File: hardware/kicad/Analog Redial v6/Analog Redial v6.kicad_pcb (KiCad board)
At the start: 2 copper layers, 115 x 52 mm, 76 parts, among them J1 Barrel_Jack_PTH_Slot, J2 PINHD_1x8_Male, J3 PINHD_1x2_Male, J4 PINHD_1x2_Male, J5 PINHD_2x4_Male, J7 PINHD_1x3_Male, J8 RJ12, J9 RJ12, U1 ESP32-C6-DevKitC-1, U2 ES8388, U3 AG1171, U4 AG1171, U5 XC6206PxxxMR

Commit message: v6 board: layout and schematic updates, PCBWay production files (Oct 5)
Co-Authored-By: Claude Sonnet 5.5 <noreply@anthropic.com>
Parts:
- removed REF**: OSHW-Logo2_14.6x12mm_SilkScreen, Symbol:OSHW-Logo2_14.6x12mm_SilkScreen
- Card1: value TF-01A -> TF-SMD_TF-01A; footprint JLCImport:TF-01A -> EasyEDA2Kicad:TF-SMD_TF-01A
- U5: value XC6206PxxxMR -> XC6206P362MR
- moved C19 9.90 mm to (108.6, 63.9)
- moved C24 4.83 mm to (71.0, 78.8)
- moved C22 4.75 mm to (73.6, 78.8)
- moved D2 2.50 mm to (89.0, 52.0)
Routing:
- net +5V: track 147.9 -> 150.7 mm, vias 8 -> 7
- net Net-(D2-A): track 20.2 -> 22.7 mm
- net /Line1_PD: track 28.1 -> 25.6 mm
- net GND: vias 102 -> 101
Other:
- board text added: "Analog Redial 6"
- board text added: "Analog Redial v6"
- board text added: "Bluetooth"
- board text removed: "Analog Redial 5"
- board text removed: "Analog Redial 5.0 Major Hack 2026/10"

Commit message: KiCad: v6 PCB edits
Co-Authored-By: Claude Sonnet 5.5 <noreply@anthropic.com>
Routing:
- net GND: vias 101 -> 103
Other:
- board text added: "18"
- board text added: "19"
- board text added: "20"
- board text added: "21"
- board text added: "Wide esp32 cut -> short ->"
- board text added: "Wide esp32 short -> cut ->"
- board text removed: "GPIO11~"

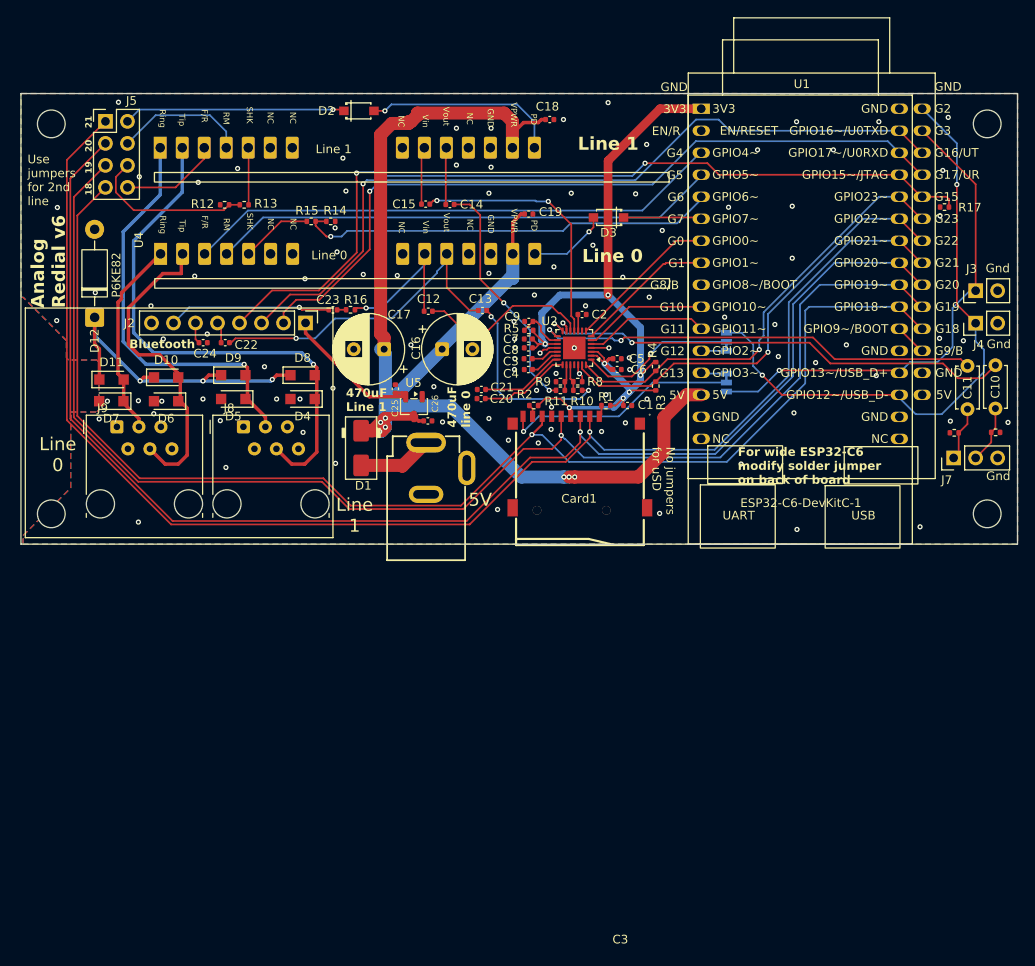
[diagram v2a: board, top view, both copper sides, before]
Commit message: v6 board released (untested): clone 5V pin fix, silkscreen updates; JLCPCB export files; docs say untested but should work
U5 stays the 3.3 V XC6206P332MR (JLC Basic); the 3.6 V part was not done.

Co-Authored-By: Claude Sonnet 5.5 <noreply@anthropic.com>
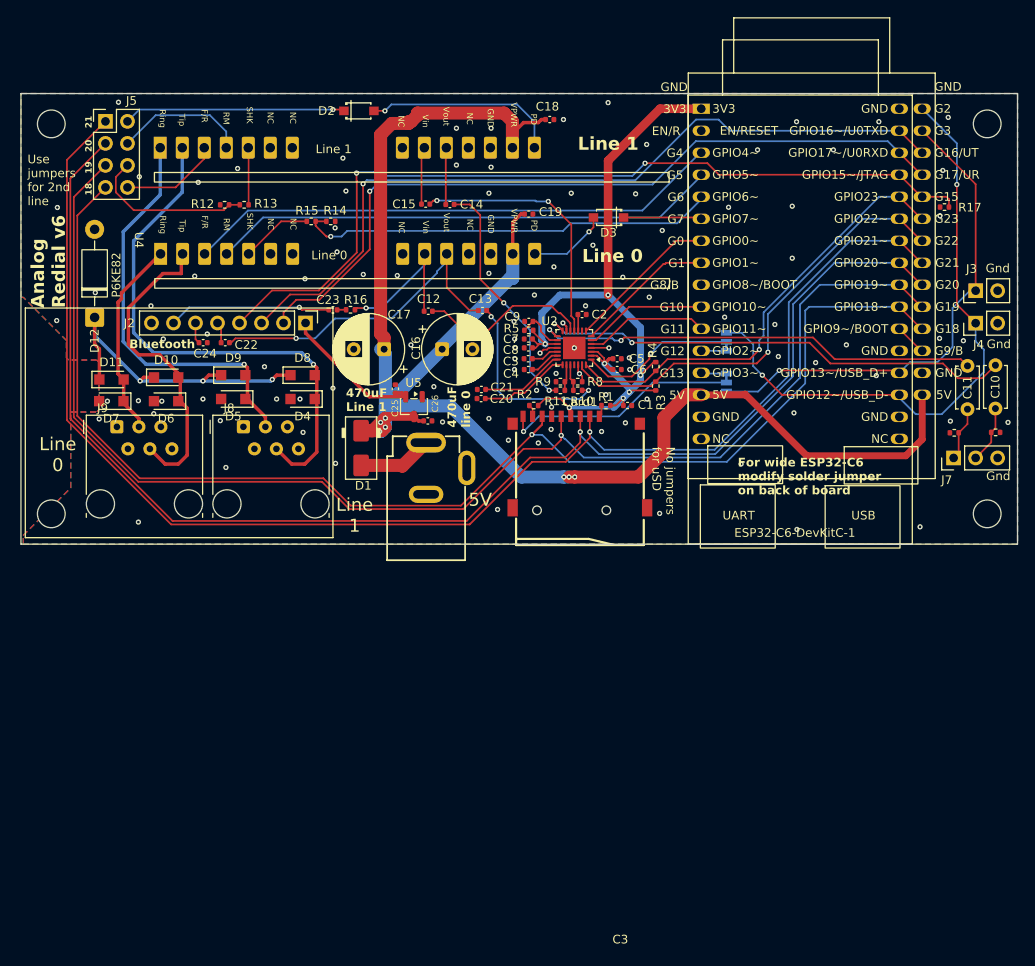
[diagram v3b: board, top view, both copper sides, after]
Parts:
- Card1: value TF-SMD_TF-01A -> TF-01A; footprint EasyEDA2Kicad:TF-SMD_TF-01A -> Custom:TF-01A
- U5: value XC6206P362MR -> XC6206P332MR
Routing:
- net +5V: track 150.7 -> 185.1 mm

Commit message: v6: +5V and +3.3V vias to 0.8/0.4 where they fit (4 stay 0.6/0.3); Power net class gets 0.8/0.4 vias and +3.3V
Co-Authored-By: Claude Sonnet 5.5 <noreply@anthropic.com>
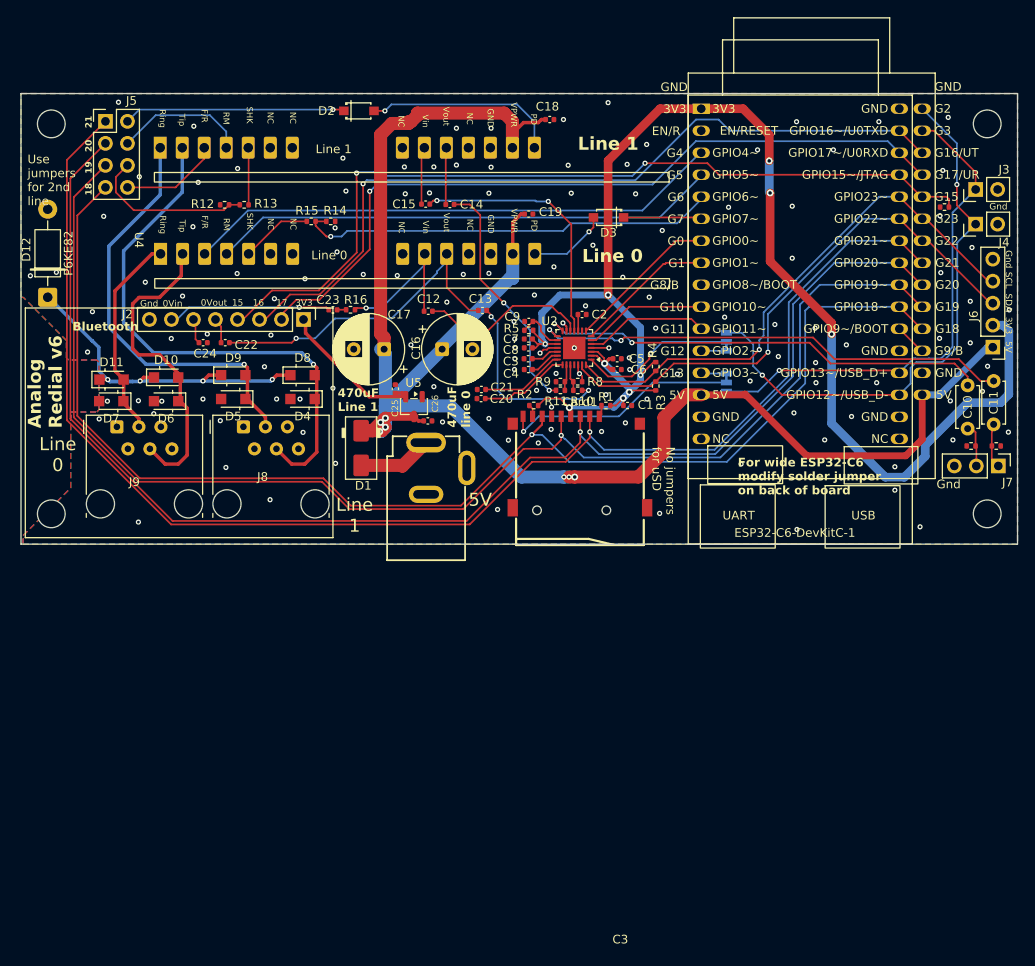
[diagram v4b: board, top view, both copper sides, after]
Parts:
- added J6: PINHD_1x5_Male, Connector_PinHeader_2.54mm:PinHeader_1x05_P2.54mm_Vertical, F.Cu at (162.1, 79.3)
- moved J3 11.7 mm to (160.2, 61.1)
- moved J4 11.4 mm to (160.2, 65.1)
- moved D12 5.89 mm to (53.1, 73.5)
- moved J7 5.24 mm to (162.8, 93.0), turned to -90 degrees
- moved R7 5.08 mm to (162.5, 90.7), turned to 0 degrees
- moved C10 3.96 mm to (159.2, 88.7)
- moved C11 3.49 mm to (162.2, 88.2)
- moved R6 3.24 mm to (159.6, 90.7), turned to 0 degrees
- moved J2 0.47 mm to (82.6, 76.1)
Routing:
- net +3.3V: track 93.3 -> 175.9 mm, vias 7 -> 10
- net /I2C_SCL: track 51.7 -> 62.9 mm
- net /I2C_SDA: track 52.2 -> 63.3 mm
- net +5V: track 185.1 -> 195.5 mm
- net /GPIO12: track 71.5 -> 66.6 mm
- net Net-(U2-LOUT2): track 51.5 -> 55.2 mm
- net /P6K: track 38.0 -> 41.3 mm, vias 3 -> 4
- net Net-(U2-ROUT2): track 55.5 -> 52.6 mm
- net Net-(C11-Pad1): track 7.08 -> 5.20 mm
- net Net-(C10-Pad1): track 6.70 -> 5.01 mm
- net /Line2Ring: track 47.4 -> 48.8 mm
- net /Line2Tip: track 62.2 -> 63.1 mm
- net /Line1Ring: track 23.0 -> 23.9 mm
- net GND: vias 103 -> 135
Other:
- board text added: "0Vin"
- board text added: "0Vout"
- board text added: "15"
- board text added: "16"
- board text added: "17"
- board text added: "SCL"
- board text added: "SDA"

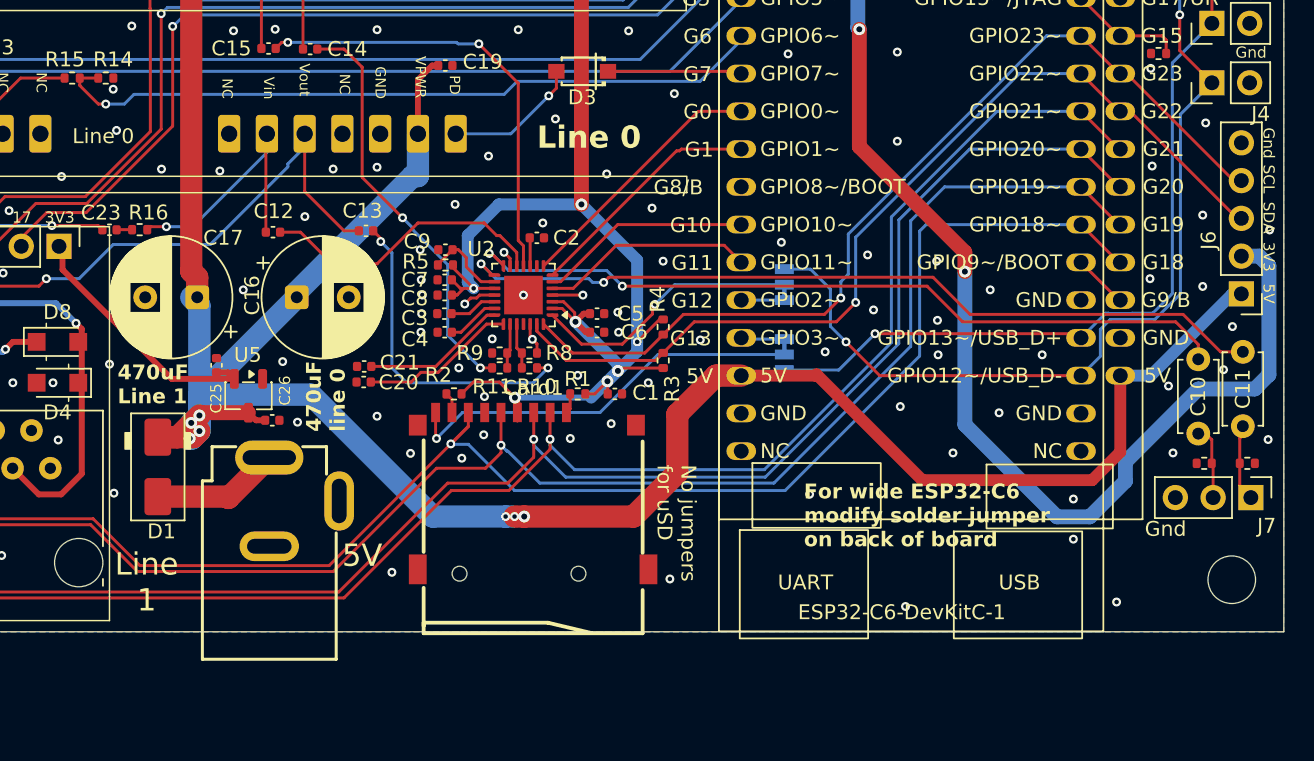
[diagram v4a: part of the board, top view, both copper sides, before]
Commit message: v6 KiCad files and exports (SS34 D1, larger power vias, teardrops); PayPhone project and cards; README: fix the v5 board image name (case); ignore KiCad local history and editor backups
Co-Authored-By: Claude Sonnet 5.5 <noreply@anthropic.com>
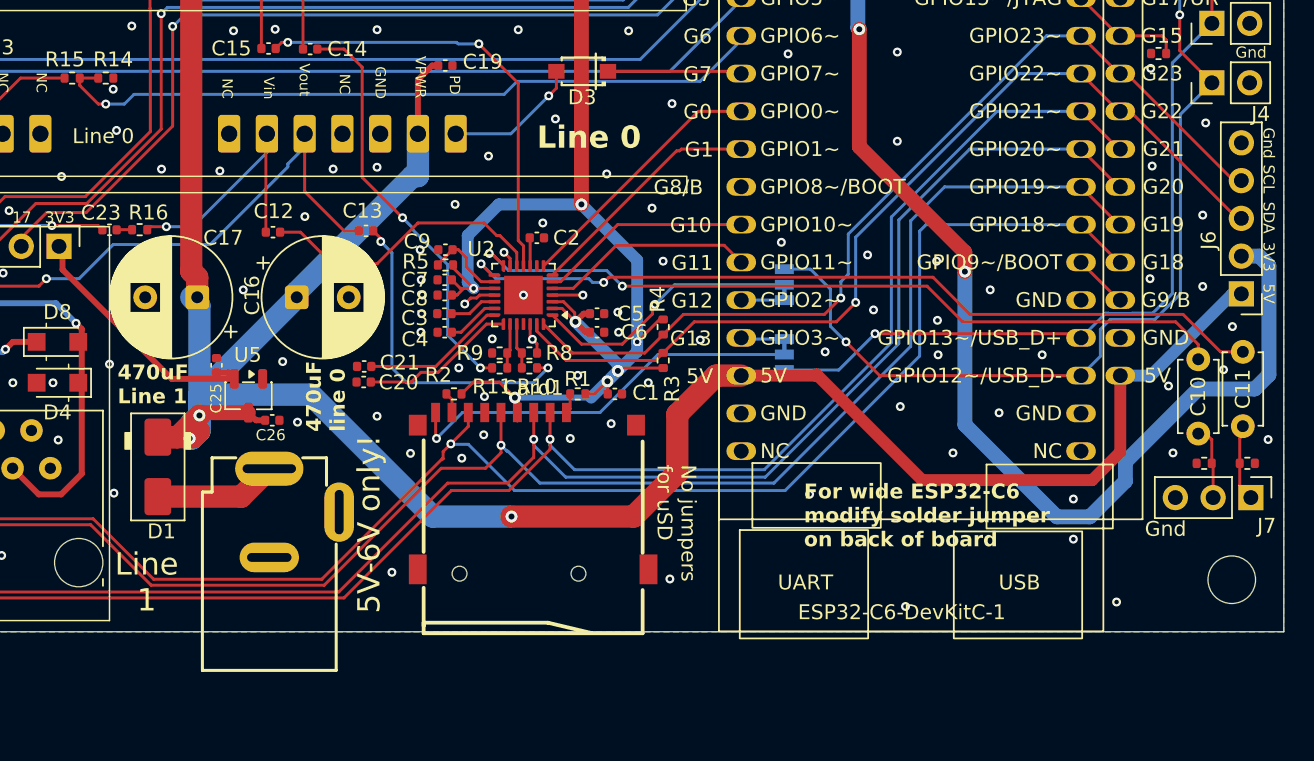
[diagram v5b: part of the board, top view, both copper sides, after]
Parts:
- D1: value SS14 -> SS34
- U5: value XC6206P332MR -> XC6206P362MR
- moved J1 0.75 mm to (96.8, 97.0)
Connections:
- net +3.3V_BM renamed +3.6V_BM
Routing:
- net /SD_CLK: track 154.2 -> 155.0 mm
- net /SD_MISO: track 151.8 -> 151.2 mm
- net GND: vias 135 -> 134
- net +5V: vias 7 -> 3
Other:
- board text added: "5V-6V only!"
